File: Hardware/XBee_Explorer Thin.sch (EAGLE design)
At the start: 64 parts, among them J4 QWIIC_RIGHT_ANGLE, Q2 3.1A/30V/105mΩ, U1 FSUSB30MUX_MSOP10, U2 AP63203, U3 ESD Diode, U5 ESD Diode, U6 CP210X

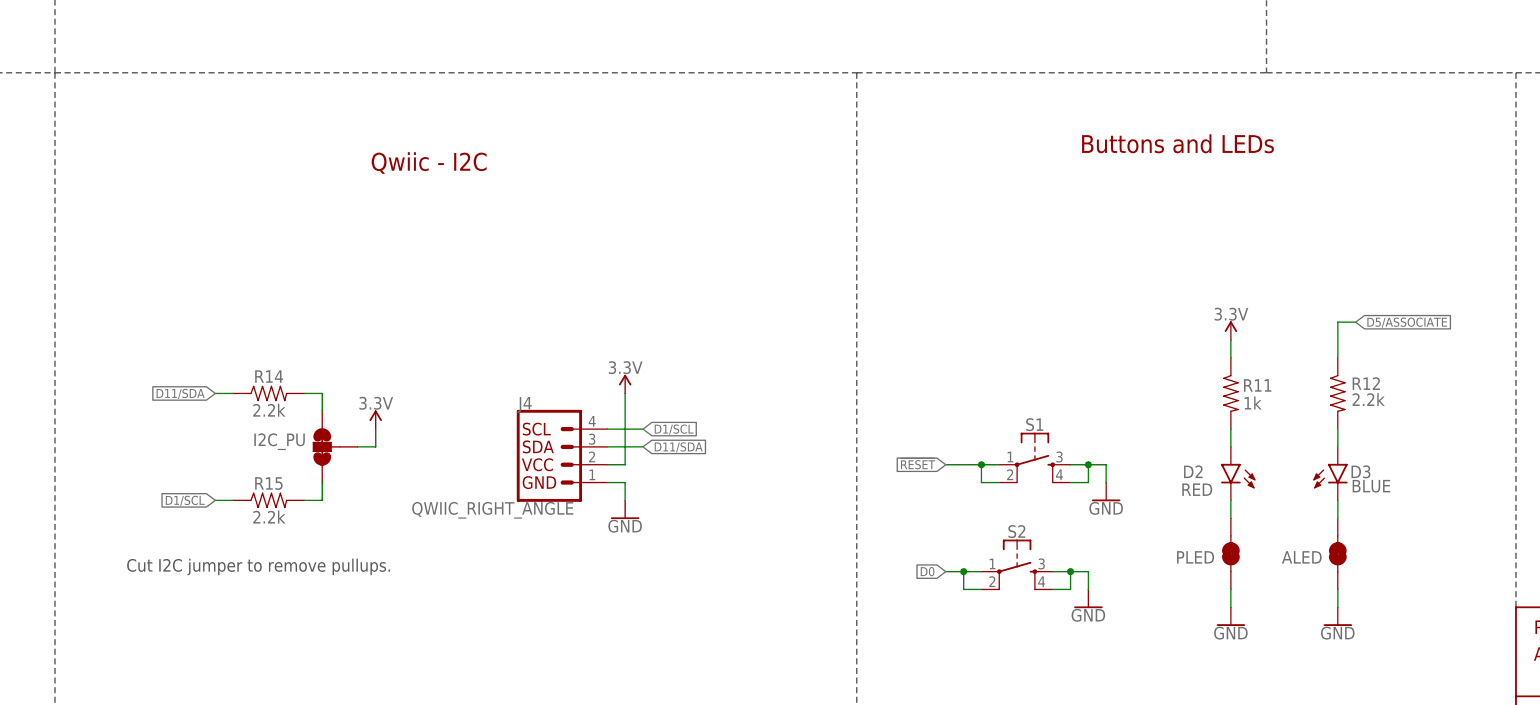
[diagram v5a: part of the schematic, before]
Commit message: Adds text for LED jumpers
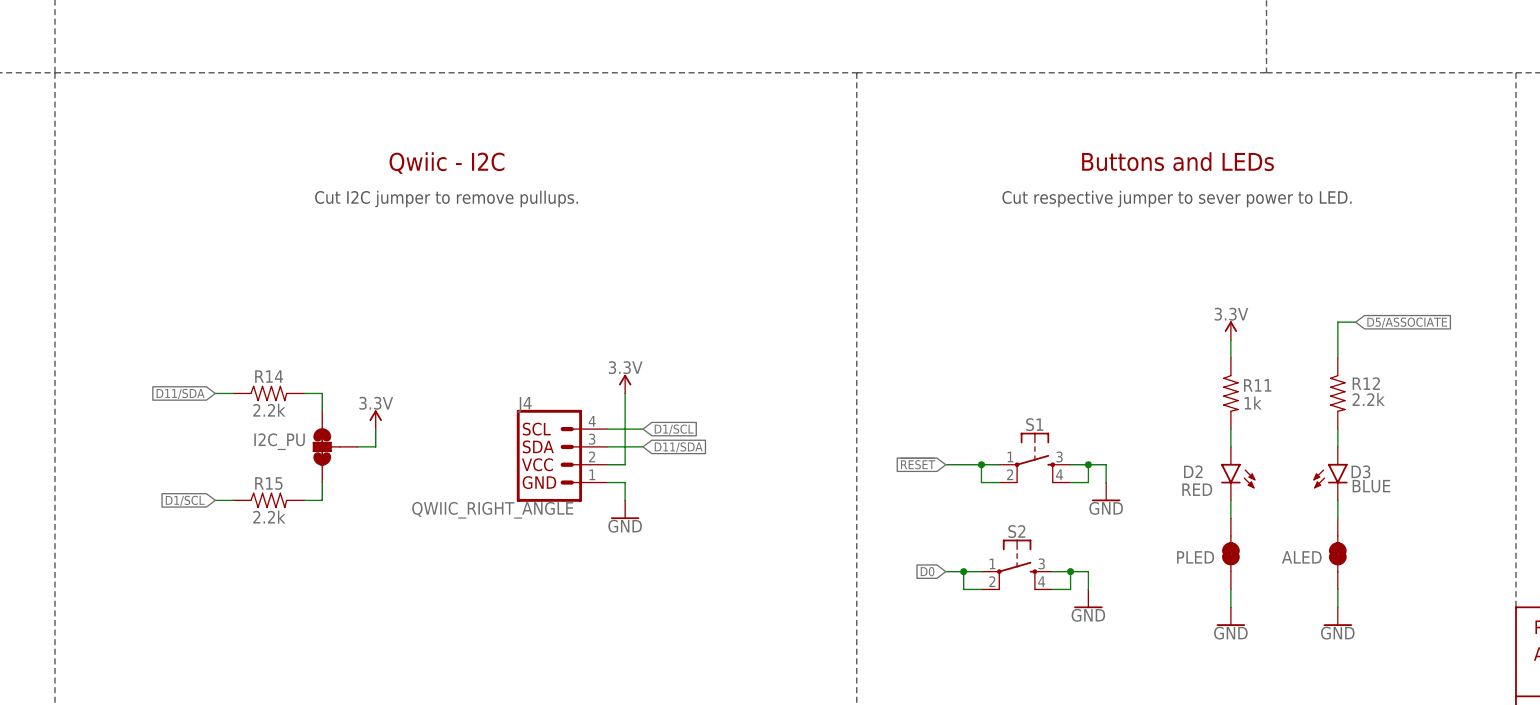
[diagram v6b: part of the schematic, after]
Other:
- note added: "Cut respective jumper to sever power to LED."
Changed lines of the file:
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@@
 USB Shields from Ground. </text>
 <text x="60.96" y="269.24" size="2.54" layer="94" font="vector" align="center">XBee Headers</text>
-<text x="175.26" y="99.06" size="2.54" layer="94" font="vector" align="center">Qwiic - I2C</text>
+<text x="177.8" y="99.06" size="2.54" layer="94" font="vector" align="center">Qwiic - I2C</text>
 <wire x1="0" y1="111.76" x2="121.92" y2="111.76" width="0.2032" layer="97" style="longdash"/>
 <wire x1="121.92" y1="111.76" x2="121.92" y2="208.28" width="0.2032" layer="97" style="longdash"/>
@@
 <text x="58.42" y="91.44" size="1.778" layer="97" font="vector" align="center">Default (Low) = I2C (SDA)</text>
 <wire x1="330.2" y1="111.76" x2="330.2" y2="35.56" width="0.2032" layer="97" style="longdash"/>
-<text x="281.94" y="101.6" size="2.54" layer="94" font="vector" align="center">Buttons and LEDs</text>
+<text x="281.94" y="99.06" size="2.54" layer="94" font="vector" align="center">Buttons and LEDs</text>
 <text x="195.58" y="187.96" size="1.778" layer="97" font="vector">VIN: 3.8 - 5.5V
 Iout: 2A Max</text>
 <text x="200.66" y="269.24" size="2.54" layer="94" font="vector" align="center">USB-C Connectors</text>
 <wire x1="121.92" y1="208.28" x2="294.64" y2="208.28" width="0.1524" layer="97" style="longdash"/>
-<text x="132.08" y="40.64" size="1.778" layer="97" font="vector">Cut I2C jumper to remove pullups.</text>
+<text x="177.8" y="93.98" size="1.778" layer="97" font="vector" align="center">Cut I2C jumper to remove pullups.</text>
+<text x="281.94" y="93.98" size="1.778" layer="97" font="vector" align="center">Cut respective jumper to sever power to LED.</text>
 </plain>
 <instances>
